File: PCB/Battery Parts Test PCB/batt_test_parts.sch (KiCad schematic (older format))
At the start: 14 parts, among them U1 ISL94203

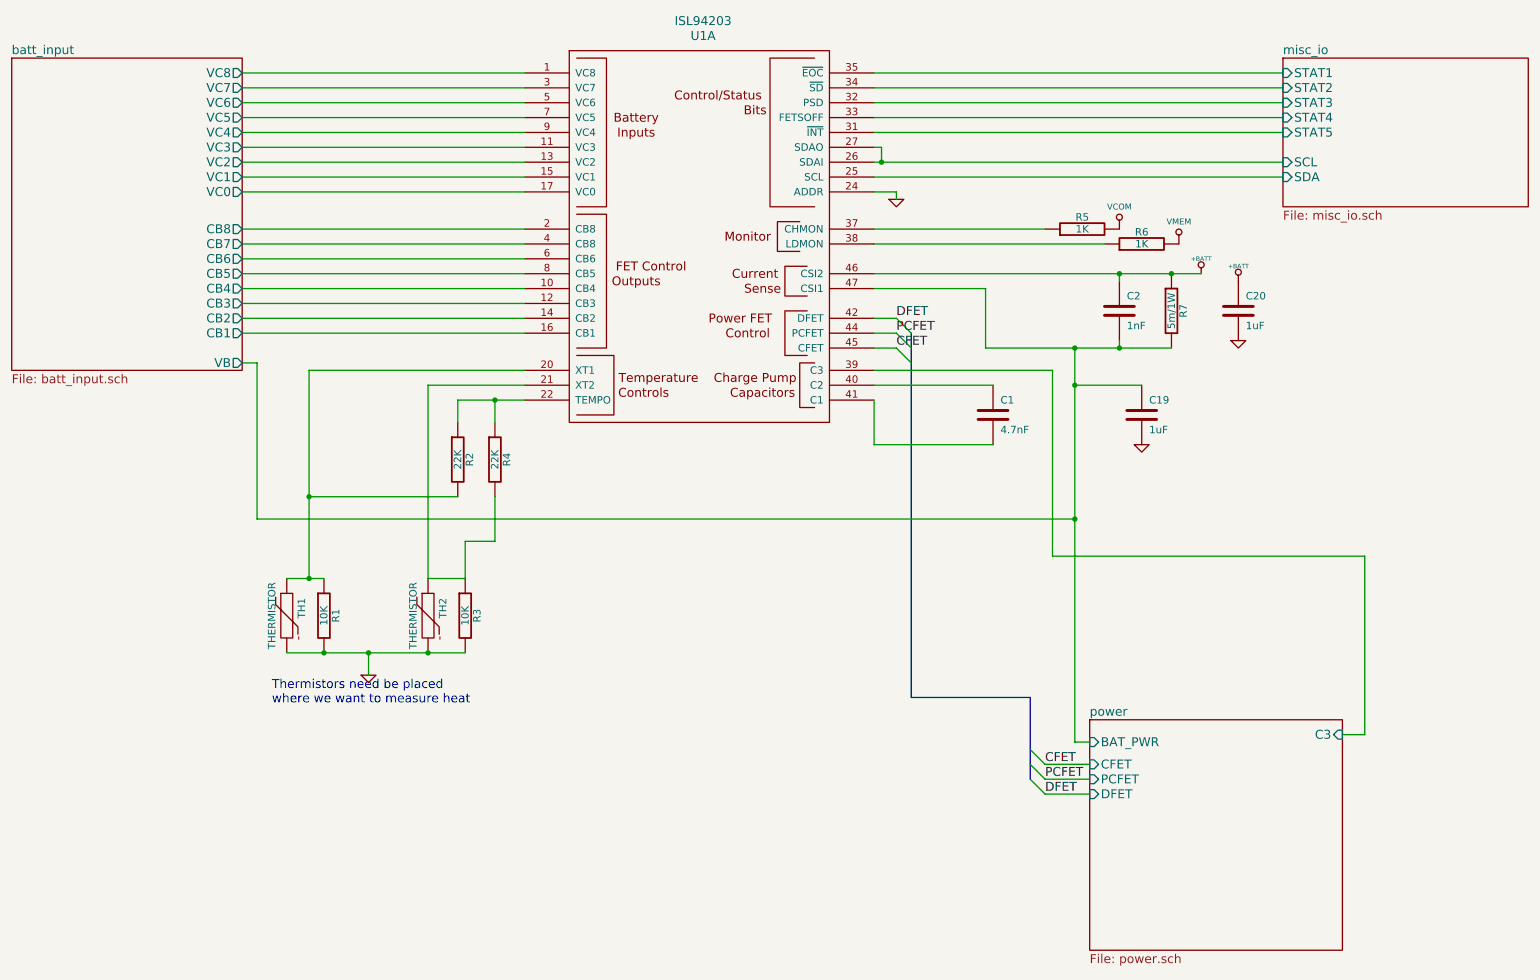
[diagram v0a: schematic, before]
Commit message: finished schematic with new battery monitor
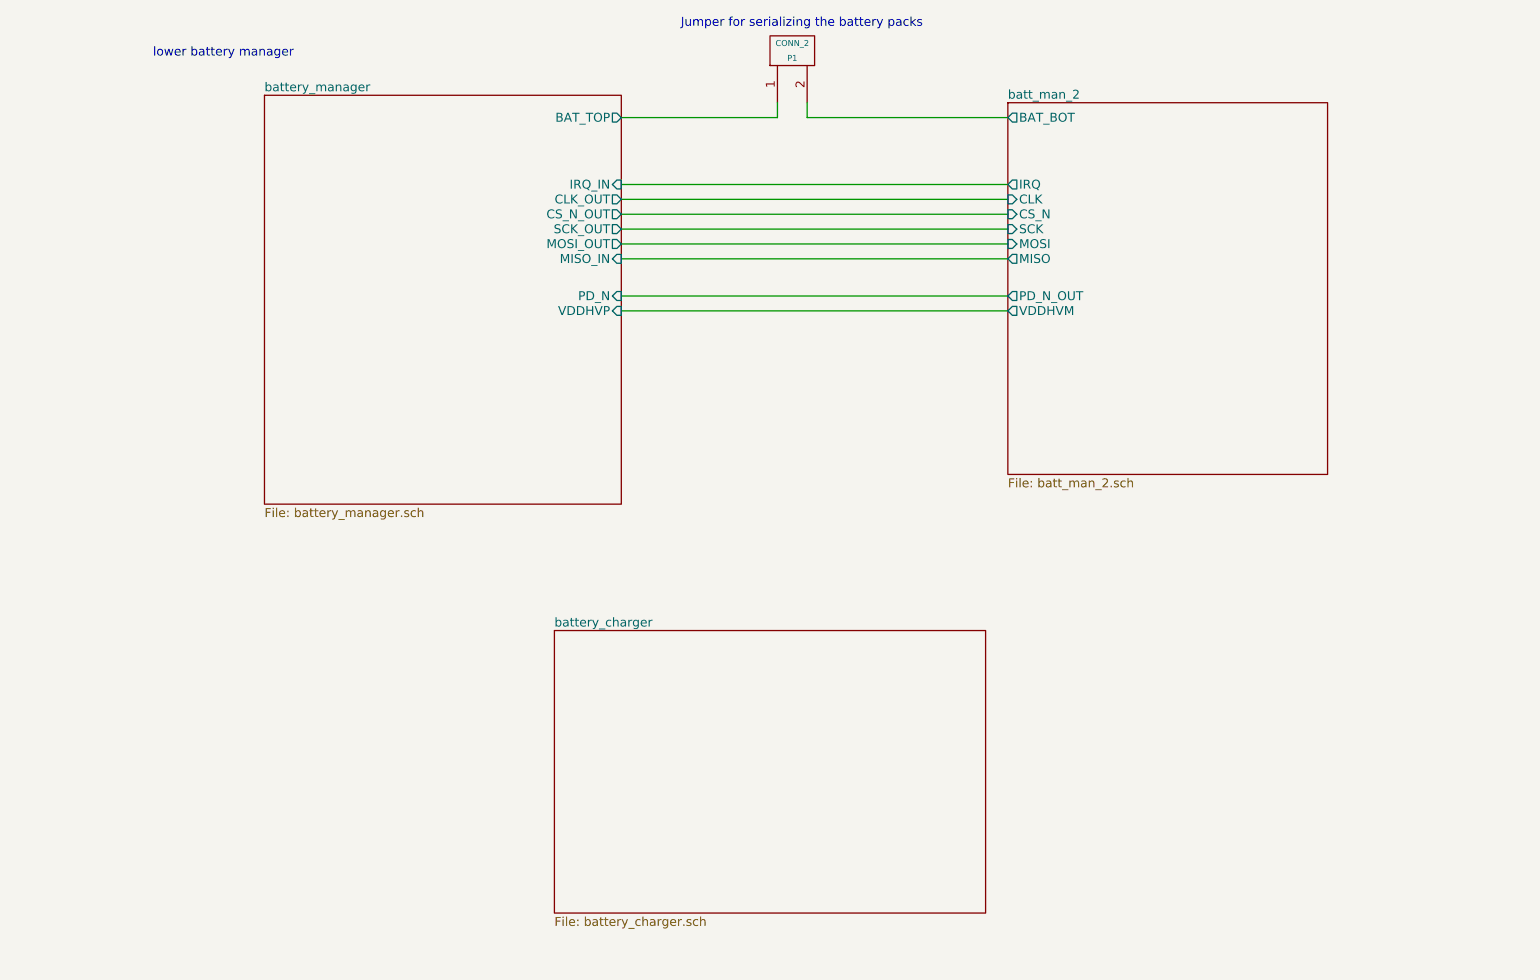
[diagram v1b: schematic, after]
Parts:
- removed C1: 4.7nF, symbol C
- removed C19, C20: 1uF, symbol C
- removed C2: 1nF, symbol C
- removed R1, R3: 10K, symbol R
- removed R2, R4: 22K, symbol R
- removed R5, R6: 1K, symbol R
- removed R7: 5m/1W, symbol R
- removed TH1, TH2: THERMISTOR, symbol THERMISTOR
- removed U1: ISL94203, symbol ISL94203
- added P1: CONN_2, symbol CONN_2
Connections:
- new net batt_man_2/BAT_BOT: P1.2 (PM)
- new net battery_manager/BAT_TOP: P1.1 (P1)
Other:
- note added: "Jumper for serializing the battery packs"
- note added: "lower battery manager"
- note removed: "Thermistors need be placed \nwhere we want to measure heat"
